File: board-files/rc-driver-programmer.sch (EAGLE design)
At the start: 14 parts, among them IC1 TINY22S

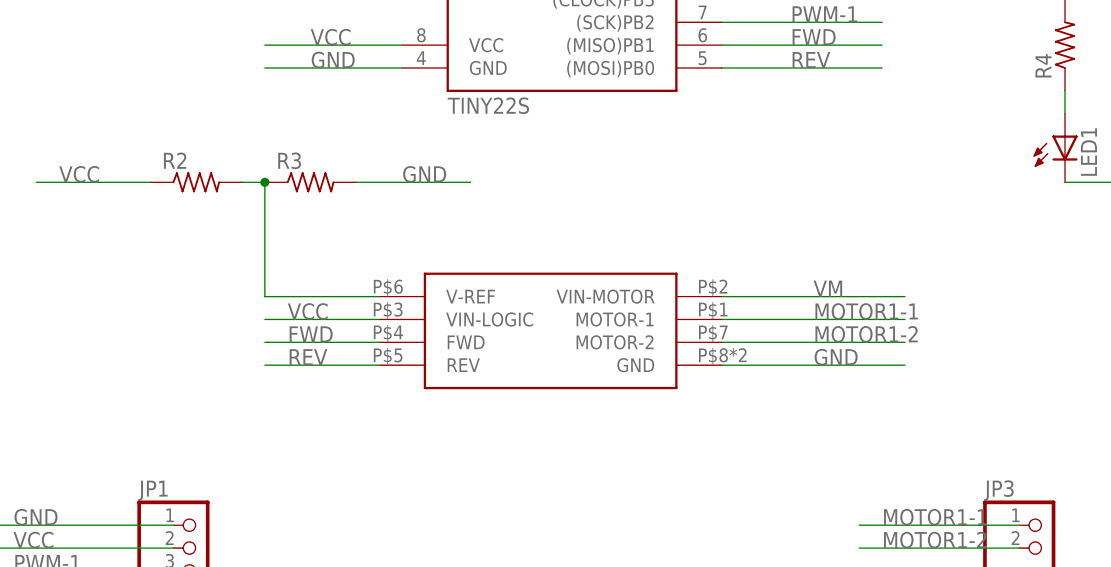
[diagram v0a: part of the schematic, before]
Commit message: Adding RC net to VREF. Creating gerbers for plain board.
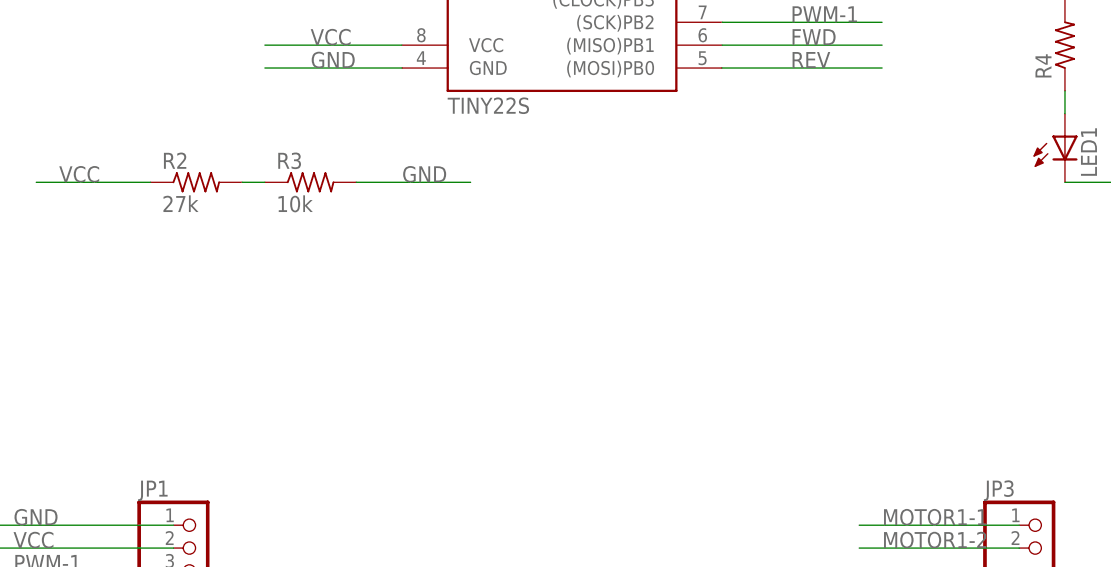
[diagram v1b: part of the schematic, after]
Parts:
- removed U$1: ZXBM5210-MOTOR-DRIVER, mgregg:ZXBM5210-MOTOR-DRIVER
- R2: value (none) -> 27k
- R3: value (none) -> 10k
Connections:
- removed net N$1: R2.2, R3.1, U$1.V-REF
- new net N$4: R2.2, R3.1
- net FWD: no longer U$1.FWD
- net GND: no longer U$1.GND
- net MOTOR1-1: no longer U$1.MOTOR-1
- net MOTOR1-2: no longer U$1.MOTOR-2
- net REV: no longer U$1.REV
- net VCC: no longer U$1.VIN-LOGIC
- net VM: no longer U$1.VIN-MOTOR
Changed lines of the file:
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@@
 <part name="JP1" library="pinhead" deviceset="PINHD-1X3" device=""/>
 <part name="JP3" library="pinhead" deviceset="PINHD-1X2" device=""/>
-<part name="U$1" library="mgregg" deviceset="ZXBM5210-MOTOR-DRIVER" device=""/>
 <part name="IC1" library="mgregg" deviceset="TINY22" device="S"/>
 <part name="THERM1" library="resistor" deviceset="R-US_" device="R0603" value="4.7k"/>
 <part name="R1" library="resistor" deviceset="R-US_" device="R0603" value="20k"/>
-<part name="R2" library="resistor" deviceset="R-US_" device="R0603"/>
-<part name="R3" library="resistor" deviceset="R-US_" device="R0603"/>
+<part name="R2" library="resistor" deviceset="R-US_" device="R0603" value="27k"/>
+<part name="R3" library="resistor" deviceset="R-US_" device="R0603" value="10k"/>
 <part name="R4" library="resistor" deviceset="R-US_" device="R0603"/>
 <part name="LED1" library="led" deviceset="LED" device="CHIP-LED0603"/>
@@
 <instance part="JP1" gate="A" x="-40.64" y="-2.54"/>
 <instance part="JP3" gate="G$1" x="53.34" y="-2.54"/>
-<instance part="U$1" gate="G$1" x="-2.54" y="22.86"/>
 <instance part="IC1" gate="G$1" x="0" y="55.88"/>
 <instance part="THERM1" gate="G$1" x="-40.64" y="76.2"/>
@@
 </segment>
 <segment>
-<pinref part="U$1" gate="G$1" pin="GND"/>
-<wire x1="17.78" y1="17.78" x2="38.1" y2="17.78" width="0.1524" layer="91"/>
-<label x="27.94" y="17.78" size="1.778" layer="95"/>
-</segment>
-<segment>
 <pinref part="R1" gate="G$1" pin="2"/>
 <wire x1="-22.86" y1="76.2" x2="-10.16" y2="76.2" width="0.1524" layer="91"/>
@@
 </segment>
 <segment>
-<pinref part="U$1" gate="G$1" pin="VIN-MOTOR"/>
-<wire x1="17.78" y1="25.4" x2="38.1" y2="25.4" width="0.1524" layer="91"/>
-<label x="27.94" y="25.4" size="1.778" layer="95"/>
-</segment>
-<segment>
 <pinref part="JP2" gate="G$1" pin="1"/>
 <wire x1="20.32" y1="-15.24" x2="-2.54" y2="-15.24" width="0.1524" layer="91"/>
@@
 </segment>
 <segment>
-<pinref part="U$1" gate="G$1" pin="VIN-LOGIC"/>
-<wire x1="-20.32" y1="22.86" x2="-33.02" y2="22.86" width="0.1524" layer="91"/>
-<label x="-30.48" y="22.86" size="1.778" layer="95"/>
-</segment>
-<segment>
 <pinref part="THERM1" gate="G$1" pin="1"/>
 <wire x1="-45.72" y1="76.2" x2="-55.88" y2="76.2" width="0.1524" layer="91"/>
@@
 <label x="35.56" y="-2.54" size="1.778" layer="95"/>
 </segment>
-<segment>
-<pinref part="U$1" gate="G$1" pin="MOTOR-2"/>
-<wire x1="17.78" y1="20.32" x2="38.1" y2="20.32" width="0.1524" layer="91"/>
-<label x="27.94" y="20.32" size="1.778" layer="95"/>
-</segment>
 </net>
 <net name="MOTOR1-1" class="0">
@@
 <label x="35.56" y="0" size="1.778" layer="95"/>
 </segment>
-<segment>
-<pinref part="U$1" gate="G$1" pin="MOTOR-1"/>
-<wire x1="17.78" y1="22.86" x2="38.1" y2="22.86" width="0.1524" layer="91"/>
-<label x="27.94" y="22.86" size="1.778" layer="95"/>
-</segment>
 </net>
 <net name="REV" class="0">
-<segment>
-<pinref part="U$1" gate="G$1" pin="REV"/>
-<wire x1="-20.32" y1="17.78" x2="-33.02" y2="17.78" width="0.1524" layer="91"/>
-<label x="-30.48" y="17.78" size="1.778" layer="95"/>
-</segment>
 <segment>
 <pinref part="IC1" gate="G$1" pin="(MOSI)PB0"/>
@@
 </net>
 <net name="FWD" class="0">
-<segment>
-<pinref part="U$1" gate="G$1" pin="FWD"/>
-<wire x1="-20.32" y1="20.32" x2="-33.02" y2="20.32" width="0.1524" layer="91"/>
-<label x="-30.48" y="20.32" size="1.778" layer="95"/>
-</segment>
 <segment>
 <pinref part="IC1" gate="G$1" pin="(MISO)PB1"/>
@@
 </segment>
 </net>
-<net name="N$1" class="0">
-<segment>
-<pinref part="U$1" gate="G$1" pin="V-REF"/>
-<pinref part="R3" gate="G$1" pin="1"/>
-<wire x1="-20.32" y1="25.4" x2="-33.02" y2="25.4" width="0.1524" layer="91"/>
-<wire x1="-33.02" y1="25.4" x2="-33.02" y2="38.1" width="0.1524" layer="91"/>
-<pinref part="R2" gate="G$1" pin="2"/>
-<wire x1="-33.02" y1="38.1" x2="-35.56" y2="38.1" width="0.1524" layer="91"/>
-<junction x="-33.02" y="38.1"/>
-</segment>
-</net>
 <net name="N$2" class="0">
 <segment>
@@
 </segment>
 </net>
+<net name="N$4" class="0">
+<segment>
+<pinref part="R2" gate="G$1" pin="2"/>
+<pinref part="R3" gate="G$1" pin="1"/>
+<wire x1="-33.02" y1="38.1" x2="-35.56" y2="38.1" width="0.1524" layer="91"/>
+</segment>
+</net>
